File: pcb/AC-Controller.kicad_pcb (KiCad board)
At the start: 2 copper layers, 66 x 67 mm, 80 parts, among them J1 Serial, J2 USB_C_Top, J3 USB_C_Bottom, Q1 AO3400A, Q2 AO3401A, Q3 AO3400A, Q4 AO3400A, Q5 AO3400A, SW1 Mode, SW2 Value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

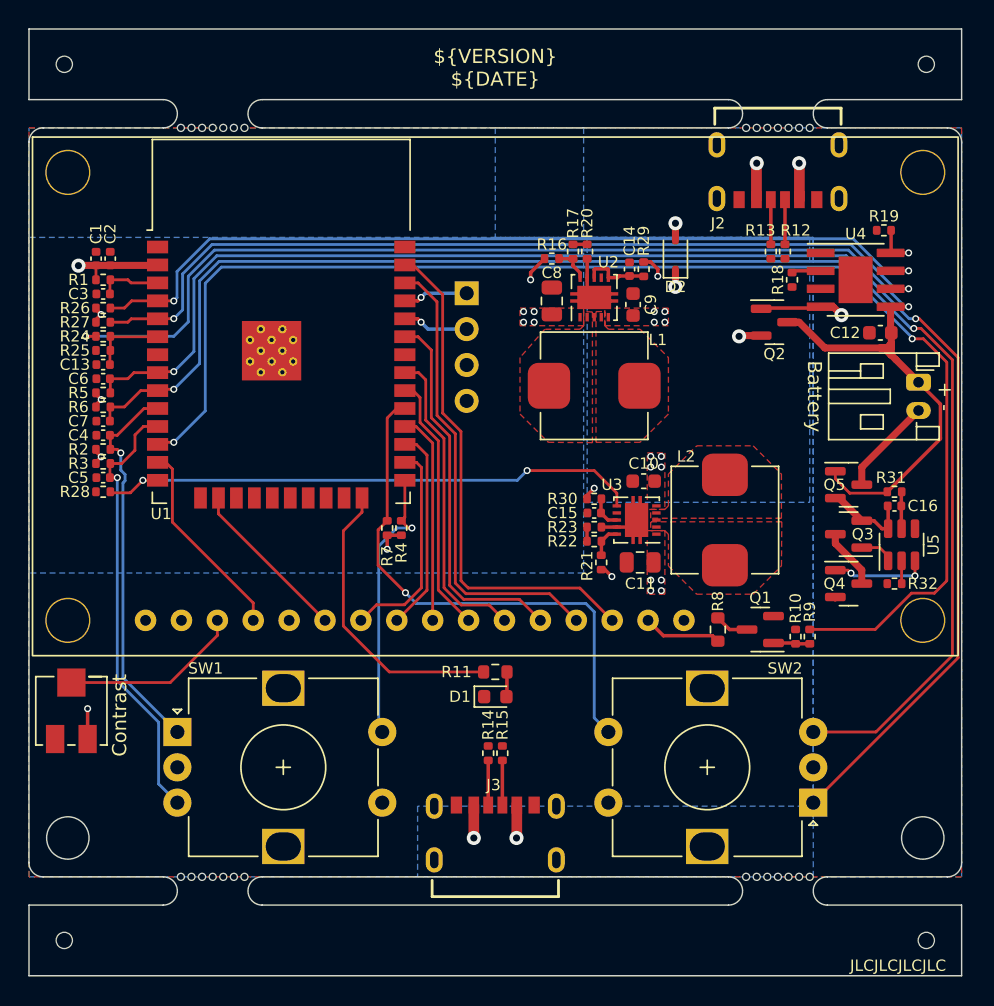
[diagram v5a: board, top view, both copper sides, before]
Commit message: fix: add missing JLC part numbers
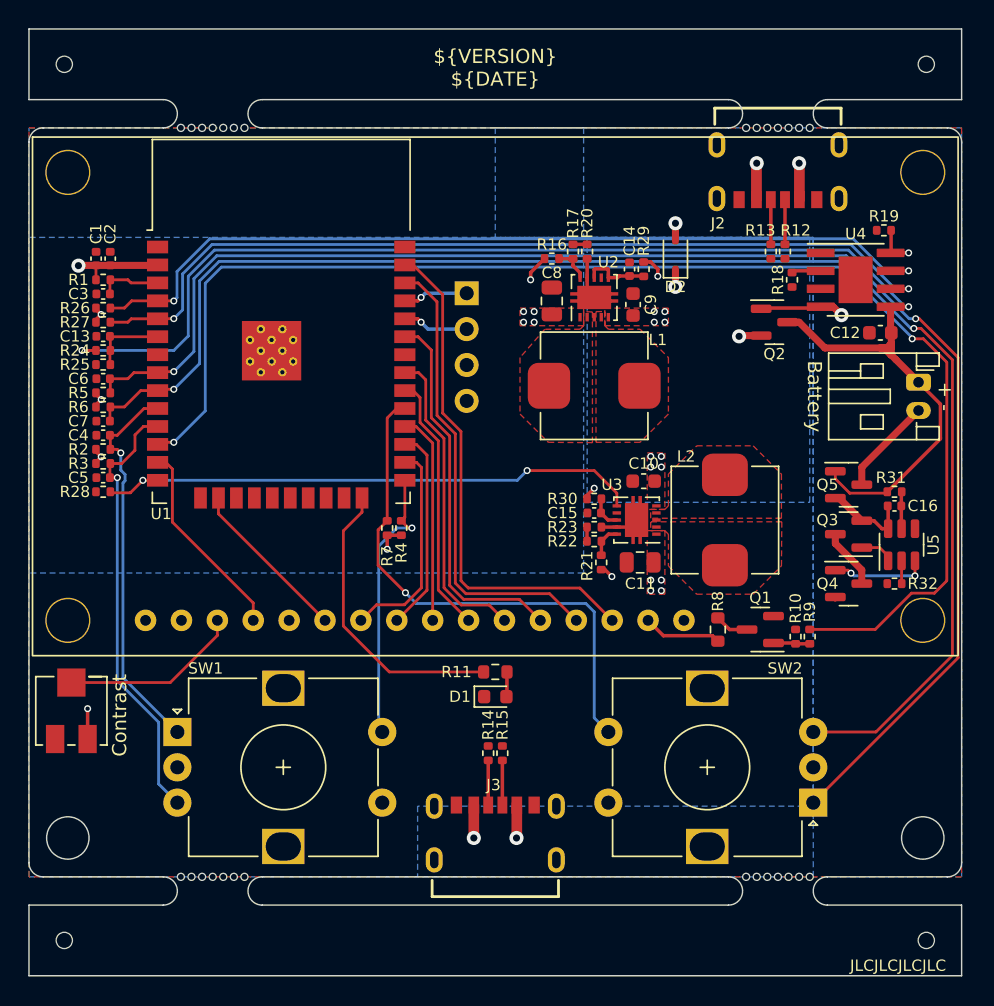
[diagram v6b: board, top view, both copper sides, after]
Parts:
- R8: value 20R -> 0R
- moved C13 2.00 mm to (122.2, 85.8)
- moved R24 1.00 mm to (122.2, 86.8)
- moved R25 1.00 mm to (122.2, 87.8)
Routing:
- net /Battery+: track 97.4 -> 98.9 mm

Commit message: feat: add Reset button
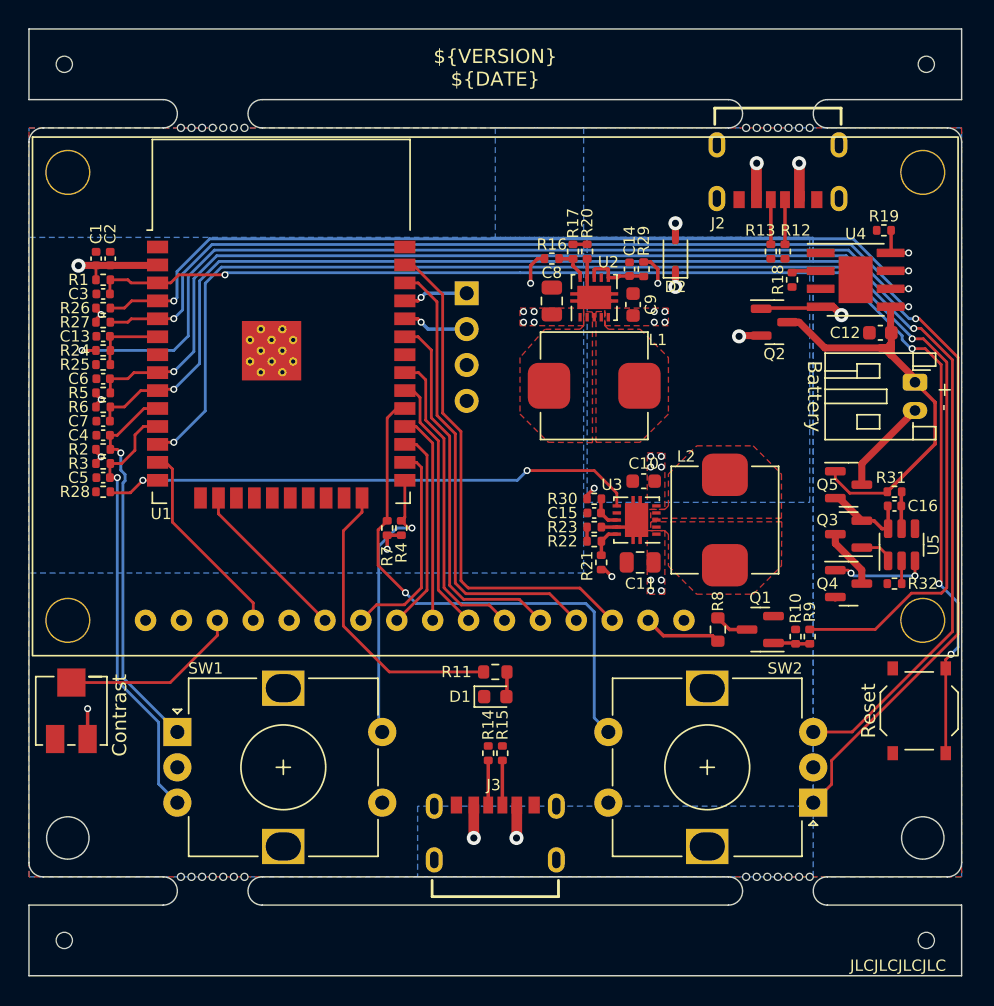
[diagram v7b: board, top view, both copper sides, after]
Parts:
- added SW3: RESET, Button_Switch_SMD:SW_Push_1P1T_XKB_TS-1187A, F.Cu at (180.0, 112.2)
- moved BT1 0.25 mm to (179.7, 89.0)
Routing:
- net /EN: track 4.40 -> 91.5 mm, vias 0 -> 4
- net /Encoder2_B: track 104.2 -> 103.2 mm
- net +3V3: track 14.5 -> 15.0 mm
- net /Power/V_{IN}: track 5.38 -> 5.88 mm
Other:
- board text added: "Reset"

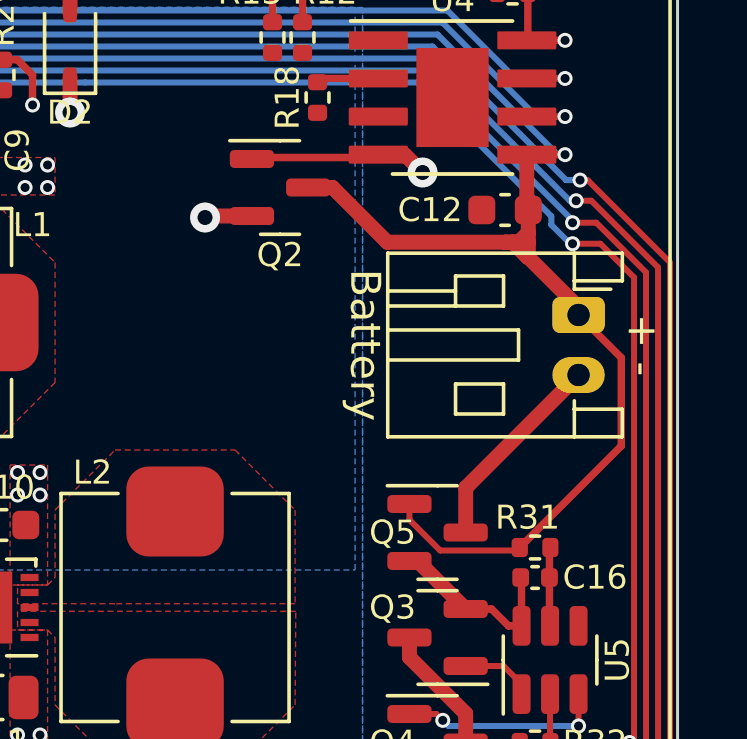
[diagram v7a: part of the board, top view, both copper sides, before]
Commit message: fix: turn around battery connector
Battery connector was not reachable with display installed
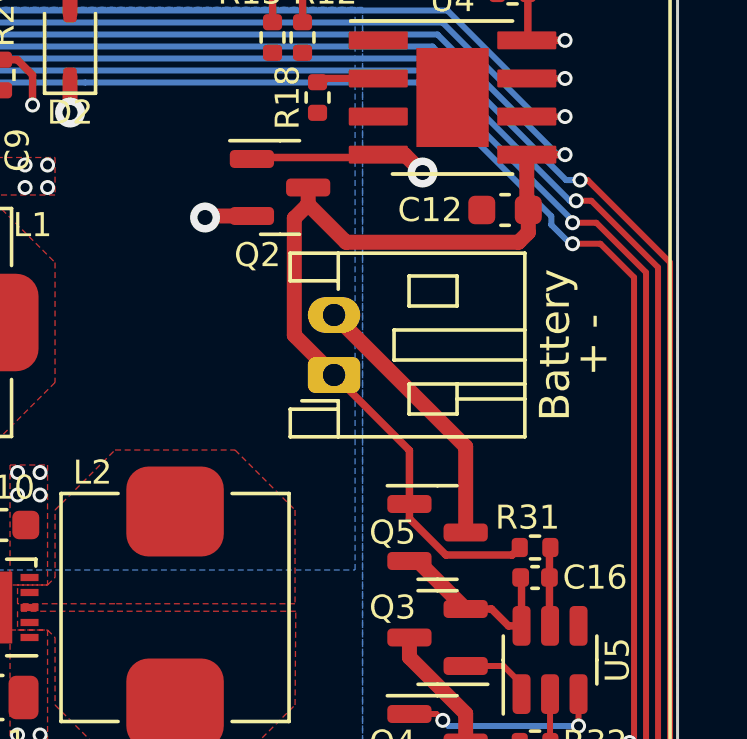
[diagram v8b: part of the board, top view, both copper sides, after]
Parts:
- moved BT1 8.39 mm to (171.6, 91.0), turned to 90 degrees
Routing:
- net /Battery+: track 98.6 -> 95.6 mm
- net /Power/B-: track 6.81 -> 9.07 mm
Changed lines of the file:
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@@
     (property "ki_keywords" "P-Channel MOSFET")
     (attr smd)
-    (fp_text reference "Q2" (at 0 2.25 180) (layer "F.SilkS")
+    (fp_text reference "Q2" (at -0.75 2.25 180) (layer "F.SilkS")
         (effects (font (size 0.8 0.8) (thickness 0.15)))
     )
@@
   )
   (footprint "Connector_JST:JST_PH_S2B-PH-K_1x02_P2.00mm_Horizontal" (layer "F.Cu")
-    (at 179.7 89 -90)
+    (at 171.55 91 90)
     (descr "JST PH series connector, S2B-PH-K (http://www.jst-mfg.com/product/pdf/eng/ePH.pdf), generated with kicad-footprint-generator")
     (tags "connector JST PH top entry")
@@
     (fp_line (start 3.95 6.25) (end 3.95 -1.35)
       (stroke (width 0.1) (type solid)) (layer "F.Fab"))
-    (pad "1" thru_hole roundrect (at 0 0 270) (size 1.2 1.75) (drill 0.75) (layers "*.Cu" "*.Mask") (roundrect_rratio 0.2083333333)
+    (pad "1" thru_hole roundrect (at 0 0 90) (size 1.2 1.75) (drill 0.75) (layers "*.Cu" "*.Mask") (roundrect_rratio 0.2083333333)
       (net 54 "/Battery+") (pinfunction "+") (pintype "passive"))
-    (pad "2" thru_hole oval (at 2 0 270) (size 1.2 1.75) (drill 0.75) (layers "*.Cu" "*.Mask")
+    (pad "2" thru_hole oval (at 2 0 90) (size 1.2 1.75) (drill 0.75) (layers "*.Cu" "*.Mask")
       (net 67 "/Power/B-") (pinfunction "-") (pintype "passive"))
     (model "${KICAD6_3DMODEL_DIR}/Connector_JST.3dshapes/JST_PH_S2B-PH-K_1x02_P2.00mm_Horizontal.wrl"
@@
     (descr "SMD Tactile Switch, http://www.helloxkb.com/public/images/pdf/TS-1187A-X-X-X.pdf")
     (tags "SPST Tactile Switch")
+    (property "LCSC" "C318884")
     (property "Sheetfile" "AC-Controller.kicad_sch")
     (property "Sheetname" "")
@@
     (effects (font (size 1 1) (thickness 0.15)) (justify right mirror))
   )
-  (gr_text "Battery" (at 172 90 270) (layer "F.SilkS")
+  (gr_text "Battery" (at 179.5 90 90) (layer "F.SilkS")
     (effects (font (size 1 1) (thickness 0.15)) (justify bottom))
   )
@@
     (effects (font (size 1 1) (thickness 0.15)) (justify left bottom))
   )
-  (gr_text "+ -" (at 181.25 90 270) (layer "F.SilkS")
+  (gr_text "+ -" (at 180.75 90 90) (layer "F.SilkS")
     (effects (font (size 1 1) (thickness 0.15)) (justify bottom))
   )
@@
   (segment (start 175.163198 79.25) (end 178.298199 82.385) (width 0.2) (layer "B.Cu") (net 53))
   (segment (start 178.298199 82.385) (end 179.25 82.385) (width 0.2) (layer "B.Cu") (net 53))
+  (segment (start 171.55 91) (end 174.0625 93.5125) (width 0.25) (layer "F.Cu") (net 54))
   (segment (start 120.75 86.75) (end 121.74 86.75) (width 0.2) (layer "F.Cu") (net 54))
-  (segment (start 178.025 87.075) (end 178 87.075) (width 0.5) (layer "F.Cu") (net 54))
-  (segment (start 178.025 87.075) (end 178.025 86.575) (width 0.5) (layer "F.Cu") (net 54))
+  (segment (start 178.025 86.25) (end 177.7 86.575) (width 0.5) (layer "F.Cu") (net 54))
+  (segment (start 170.225 85.775) (end 170.225 89.675) (width 0.5) (layer "F.Cu") (net 54))
+  (segment (start 170.6875 84.75) (end 170.6875 85.3125) (width 0.5) (layer "F.Cu") (net 54))
+  (segment (start 171.95 86.575) (end 170.6875 85.3125) (width 0.5) (layer "F.Cu") (net 54))
+  (segment (start 175.278249 97) (end 174.0625 95.784251) (width 0.25) (layer "F.Cu") (net 54))
   (segment (start 177.975 83.655) (end 177.975 85.45) (width 0.5) (layer "F.Cu") (net 54))
-  (segment (start 178.025 86.575) (end 178.025 86.25) (width 0.5) (layer "F.Cu") (net 54))
-  (segment (start 177.64 96.85) (end 175.086396 96.85) (width 0.2) (layer "F.Cu") (net 54))
-  (segment (start 179.7 89) (end 181.125 90.425) (width 0.25) (layer "F.Cu") (net 54))
-  (segment (start 179.7 89) (end 179.7 88.75) (width 0.5) (layer "F.Cu") (net 54))
-  (segment (start 174.0625 95.826104) (end 174.0625 95.3) (width 0.2) (layer "F.Cu") (net 54))
+  (segment (start 174.0625 95.784251) (end 174.0625 95.3) (width 0.25) (layer "F.Cu") (net 54))
+  (segment (start 177.49 97) (end 175.278249 97) (width 0.25) (layer "F.Cu") (net 54))
+  (segment (start 174.0625 93.5125) (end 174.0625 95.3) (width 0.25) (layer "F.Cu") (net 54))
+  (segment (start 170.225 89.675) (end 171.55 91) (width 0.5) (layer "F.Cu") (net 54))
+  (segment (start 178.025 85.5) (end 178.025 86.25) (width 0.5) (layer "F.Cu") (net 54))
   (segment (start 177.975 83.655) (end 179.25 83.655) (width 0.25) (layer "F.Cu") (net 54))
-  (segment (start 177.25 86.575) (end 177.5 86.575) (width 0.5) (layer "F.Cu") (net 54))
-  (segment (start 175.086396 96.85) (end 174.0625 95.826104) (width 0.2) (layer "F.Cu") (net 54))
-  (segment (start 181.125 90.425) (end 181.125 93.365) (width 0.25) (layer "F.Cu") (net 54))
-  (segment (start 178.025 86.25) (end 178.025 85.5) (width 0.5) (layer "F.Cu") (net 54))
-  (segment (start 181.125 93.365) (end 177.74 96.75) (width 0.25) (layer "F.Cu") (net 54))
-  (segment (start 177.25 86.575) (end 173.325 86.575) (width 0.5) (layer "F.Cu") (net 54))
-  (segment (start 177.775 86.575) (end 177.25 86.575) (width 0.5) (layer "F.Cu") (net 54))
-  (segment (start 178 87.075) (end 177.5 86.575) (width 0.5) (layer "F.Cu") (net 54))
-  (segment (start 177.7 86.575) (end 178.025 86.25) (width 0.5) (layer "F.Cu") (net 54))
-  (segment (start 178.025 86.575) (end 177.25 86.575) (width 0.5) (layer "F.Cu") (net 54))
-  (segment (start 179.7 88.75) (end 178.025 87.075) (width 0.5) (layer "F.Cu") (net 54))
-  (segment (start 177.74 96.75) (end 177.64 96.85) (width 0.2) (layer "F.Cu") (net 54))
+  (segment (start 177.74 96.75) (end 177.49 97) (width 0.25) (layer "F.Cu") (net 54))
+  (segment (start 177.7 86.575) (end 171.95 86.575) (width 0.5) (layer "F.Cu") (net 54))
   (segment (start 178.0125 85.5) (end 178.025 85.5) (width 0.5) (layer "F.Cu") (net 54))
-  (segment (start 171.5 84.75) (end 170.6875 84.75) (width 0.5) (layer "F.Cu") (net 54))
-  (segment (start 173.325 86.575) (end 171.5 84.75) (width 0.5) (layer "F.Cu") (net 54))
-  (segment (start 177.5 86.575) (end 177.7 86.575) (width 0.5) (layer "F.Cu") (net 54))
+  (segment (start 170.6875 85.3125) (end 170.225 85.775) (width 0.5) (layer "F.Cu") (net 54))
   (segment (start 177.975 85.45) (end 178.025 85.5) (width 0.5) (layer "F.Cu") (net 54))
   (via (at 120.75 86.75) (size 0.5) (drill 0.3) (layers "F.Cu" "B.Cu") (net 54))
@@
   (segment (start 165.75 105.675) (end 166.575 106.5) (width 0.25) (layer "F.Cu") (net 66))
   (segment (start 166.575 106.5) (end 167.8125 106.5) (width 0.25) (layer "F.Cu") (net 66))
-  (segment (start 175.9375 96.25) (end 175.9375 94.7625) (width 0.5) (layer "F.Cu") (net 67))
-  (segment (start 175.9375 94.7625) (end 179.7 91) (width 0.5) (layer "F.Cu") (net 67))
+  (segment (start 175.9375 93.3875) (end 171.55 89) (width 0.5) (layer "F.Cu") (net 67))
+  (segment (start 175.9375 96.25) (end 175.9375 93.3875) (width 0.5) (layer "F.Cu") (net 67))
   (segment (start 177.8 97.78) (end 177.77 97.75) (width 0.25) (layer "F.Cu") (net 68))
   (segment (start 176.8 98.8) (end 177.3625 99.3625) (width 0.25) (layer "F.Cu") (net 68))
